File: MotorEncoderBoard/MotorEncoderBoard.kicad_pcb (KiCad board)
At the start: 2 copper layers, 24.3 x 31.8 mm, 13 parts, among them P1 PWR, P2 Out, U1 RPI-579N1, U2 LM311D

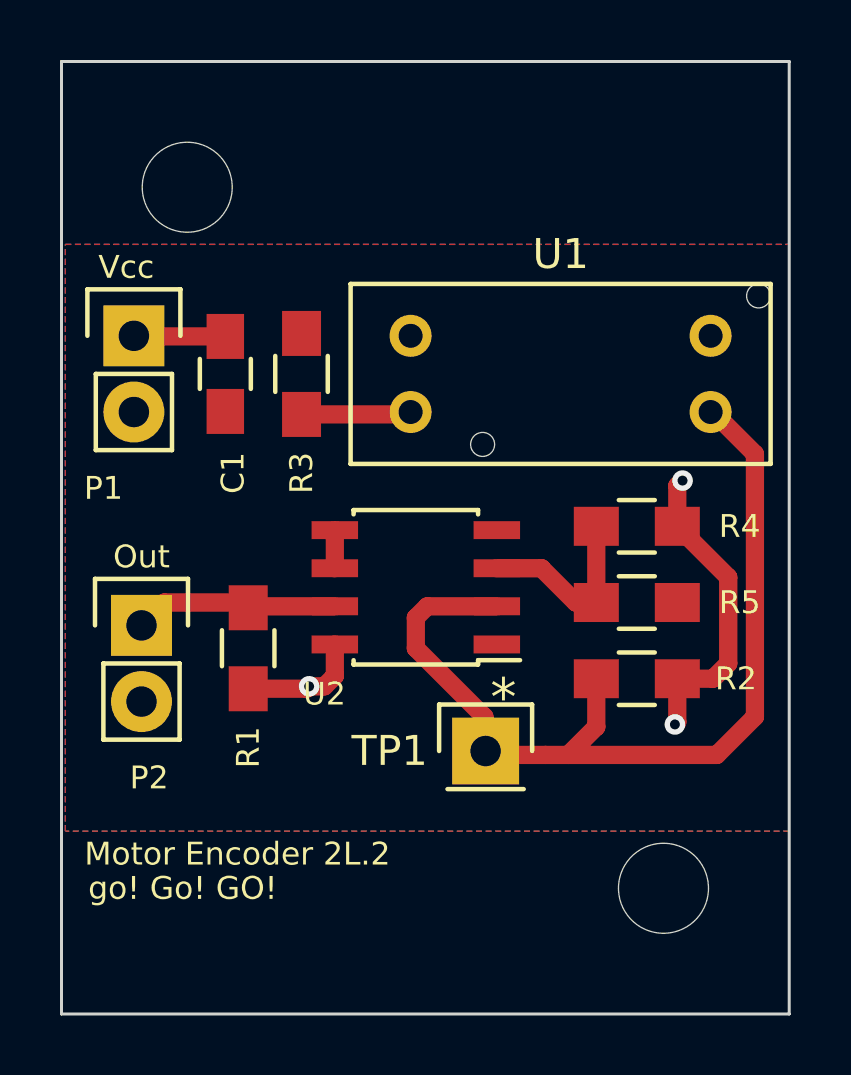
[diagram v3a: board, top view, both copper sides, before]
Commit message: Copied the Encoder Board to a new directory to start a break-out version. Created Gerbers and ordered the board 2L.3Breakout
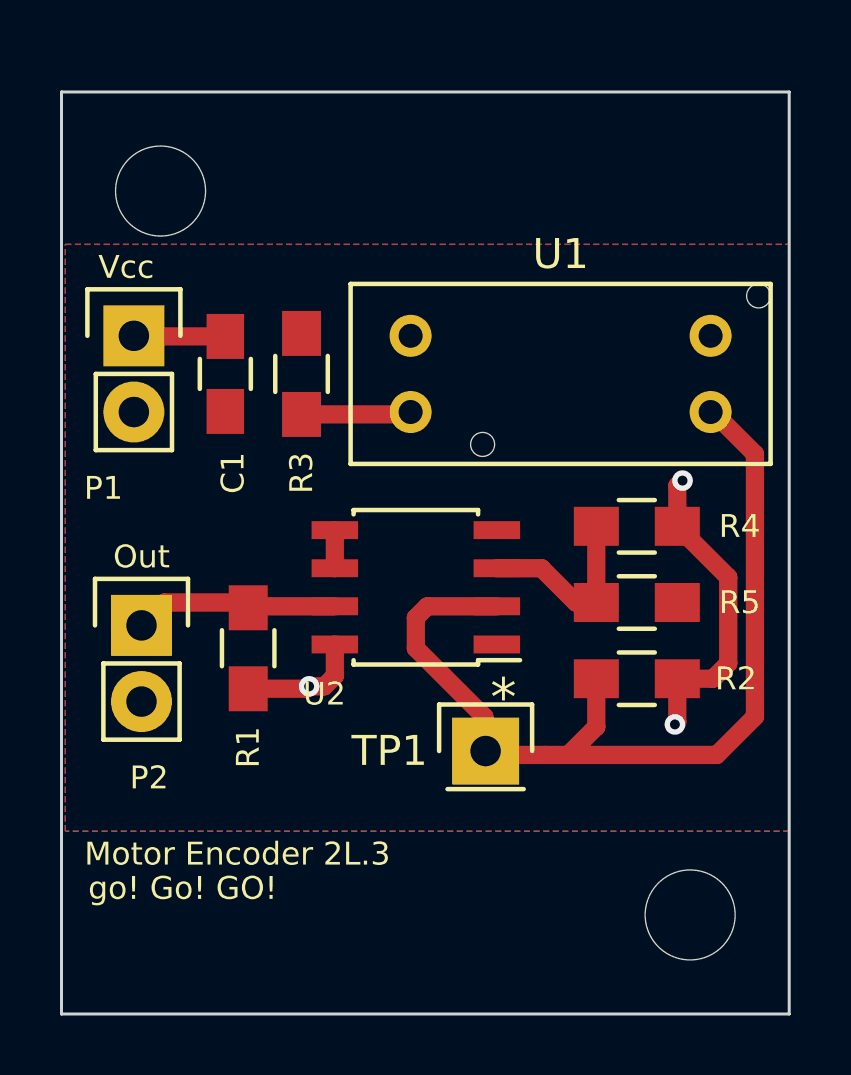
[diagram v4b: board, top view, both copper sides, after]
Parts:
- removed the REF** at (152.7, 81.4)
- removed the REF** at (168.5, 104.8)
- added REF**: MountingHole_3mm, Mounting_Holes:MountingHole_3mm, F.Cu at (169.4, 105.7)
- added REF**: MountingHole_3mm, Mounting_Holes:MountingHole_3mm, F.Cu at (151.8, 81.5)
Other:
- board size 24.3 x 31.8 mm -> 24.3 x 30.7 mm
- board text added: "Motor Encoder 2L.3"
- board text removed: "Motor Encoder 2L.2"
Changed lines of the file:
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@@
-(kicad_pcb (version 4) (host pcbnew no-vcs-found-product)
+(kicad_pcb (version 4) (host pcbnew 4.0.1-2.201512121406+6195~38~ubuntu14.04.1-stable)
   (general
     (links 22)
     (no_connects 0)
-    (area 148.412999 77.165999 172.770001 109.016001)
+    (area 144.971679 75.34104 176.206241 111.40216)
     (thickness 1.6)
-    (drawings 17)
+    (drawings 11)
     (tracks 43)
     (zones 0)
@@
   (page A4)
   (layers
-    (0 F.Cu signal)
-    (31 B.Cu signal)
+    (0 F.Cu signal hide)
+    (31 B.Cu signal hide)
     (32 B.Adhes user)
     (33 F.Adhes user)
@@
     (add_net VCC)
   )
+  (module Mounting_Holes:MountingHole_3mm (layer F.Cu)
+    (at 169.418 105.664)
+    (descr "Mounting Hole 3mm, no annular")
+    (tags "mounting hole 3mm no annular")
+    (fp_text reference REF** (at 0 -4) (layer F.SilkS) hide
+      (effects (font (size 1 1) (thickness 0.15)))
+    )
+    (fp_text value MountingHole_3mm (at 0 4) (layer F.Fab) hide
+      (effects (font (size 1 1) (thickness 0.15)))
+    )
+    (fp_circle (center 0 0) (end 3 0) (layer Cmts.User) (width 0.15))
+    (fp_circle (center 0 0) (end 3.25 0) (layer F.CrtYd) (width 0.05))
+    (pad 1 np_thru_hole circle (at 0 0) (size 3 3) (drill 3) (layers *.Cu *.Mask F.SilkS))
+  )
   (module Capacitors_SMD:C_0805_HandSoldering (layer F.Cu)
     (at 153.924 87.63 270)
@@
     )
   )
-  (module Gogogo-Footprint:MountingHole-3mm (layer F.Cu)
-    (at 152.654 81.407)
-    (fp_text reference REF** (at -0.00254 5.69976) (layer F.SilkS) hide
-      (effects (font (size 1 1) (thickness 0.15)))
-    )
-    (fp_text value MountingHole-3mm (at -0.00254 -4.98856) (layer F.Fab) hide
-      (effects (font (size 1 1) (thickness 0.15)))
-    )
-    (pad "" np_thru_hole circle (at 0 0) (size 3 3) (drill 3) (layers *.Cu *.Mask F.SilkS))
-  )
-  (module Gogogo-Footprint:MountingHole-3mm (layer F.Cu)
-    (at 168.529 104.775)
-    (fp_text reference REF** (at -0.00254 5.69976) (layer F.SilkS) hide
-      (effects (font (size 1 1) (thickness 0.15)))
-    )
-    (fp_text value MountingHole-3mm (at -0.00254 -4.98856) (layer F.Fab) hide
-      (effects (font (size 1 1) (thickness 0.15)))
-    )
-    (pad "" np_thru_hole circle (at 0 0) (size 3 3) (drill 3) (layers *.Cu *.Mask F.SilkS))
-  )
   (module Pin_Headers:Pin_Header_Straight_1x01 (layer F.Cu)
     (at 162.6 100.2)
@@
       (net 1 VCC))
   )
+  (module Mounting_Holes:MountingHole_3mm (layer F.Cu)
+    (at 151.765 81.534)
+    (descr "Mounting Hole 3mm, no annular")
+    (tags "mounting hole 3mm no annular")
+    (fp_text reference REF** (at 0 -4) (layer F.SilkS) hide
+      (effects (font (size 1 1) (thickness 0.15)))
+    )
+    (fp_text value MountingHole_3mm (at 0 4) (layer F.Fab) hide
+      (effects (font (size 1 1) (thickness 0.15)))
+    )
+    (fp_circle (center 0 0) (end 3 0) (layer Cmts.User) (width 0.15))
+    (fp_circle (center 0 0) (end 3.25 0) (layer F.CrtYd) (width 0.05))
+    (pad 1 np_thru_hole circle (at 0 0) (size 3 3) (drill 3) (layers *.Cu *.Mask F.SilkS))
+  )
   (gr_text "go! Go! GO!" (at 149.352 104.775) (layer F.SilkS)
     (effects (font (size 0.762 0.762) (thickness 0.127)) (justify left))
   )
-  (gr_text "Motor Encoder 2L.2" (at 149.225 103.632) (layer F.SilkS)
+  (gr_text "Motor Encoder 2L.3" (at 149.225 103.632) (layer F.SilkS)
     (effects (font (size 0.762 0.762) (thickness 0.127)) (justify left))
   )
   (gr_line (start 148.463 108.966) (end 172.72 108.966) (angle 90) (layer Edge.Cuts) (width 0.1))
-  (gr_line (start 148.463 108.966) (end 148.463 77.216) (angle 90) (layer Edge.Cuts) (width 0.1))
-  (gr_line (start 172.72 77.216) (end 172.72 108.966) (angle 90) (layer Edge.Cuts) (width 0.1))
-  (gr_line (start 148.463 77.216) (end 172.72 77.216) (angle 90) (layer Edge.Cuts) (width 0.1))
+  (gr_line (start 148.463 108.966) (end 148.463 78.232) (angle 90) (layer Edge.Cuts) (width 0.1))
+  (gr_line (start 172.72 78.232) (end 172.72 108.966) (angle 90) (layer Edge.Cuts) (width 0.1))
+  (gr_line (start 148.463 78.232) (end 172.72 78.232) (angle 90) (layer Edge.Cuts) (width 0.1))
   (gr_line (start 172.72 108.966) (end 168.529 108.966) (angle 90) (layer Eco1.User) (width 0.1))
   (gr_line (start 172.72 104.775) (end 172.72 108.966) (angle 90) (layer Eco1.User) (width 0.1))
-  (gr_line (start 148.463 77.216) (end 148.463 81.407) (angle 90) (layer Eco1.User) (width 0.1))
-  (gr_line (start 152.654 77.216) (end 148.463 77.216) (angle 90) (layer Eco1.User) (width 0.1))
-  (gr_line (start 152.654 81.407) (end 148.463 81.407) (angle 90) (layer Eco1.User) (width 0.1))
-  (gr_line (start 172.72 104.775) (end 168.529 104.775) (angle 90) (layer Eco1.User) (width 0.1))
-  (gr_line (start 152.654 81.407) (end 152.654 77.216) (angle 90) (layer Eco1.User) (width 0.1))
-  (gr_line (start 168.529 104.775) (end 168.529 108.966) (angle 90) (layer Eco1.User) (width 0.1))
   (gr_text Vcc (at 150.622 84.074) (layer F.SilkS)
     (effects (font (size 0.762 0.762) (thickness 0.127)))
